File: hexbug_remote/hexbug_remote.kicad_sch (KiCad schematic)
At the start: 39 parts, among them J1 USB C, J2 Conn_01x02, J3 Conn_01x06, J4 AA, J5 AA, SW1 Tactile, SW2 Tactile, SW3 Tactile, SW4 Tactile, SW5 Tactile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

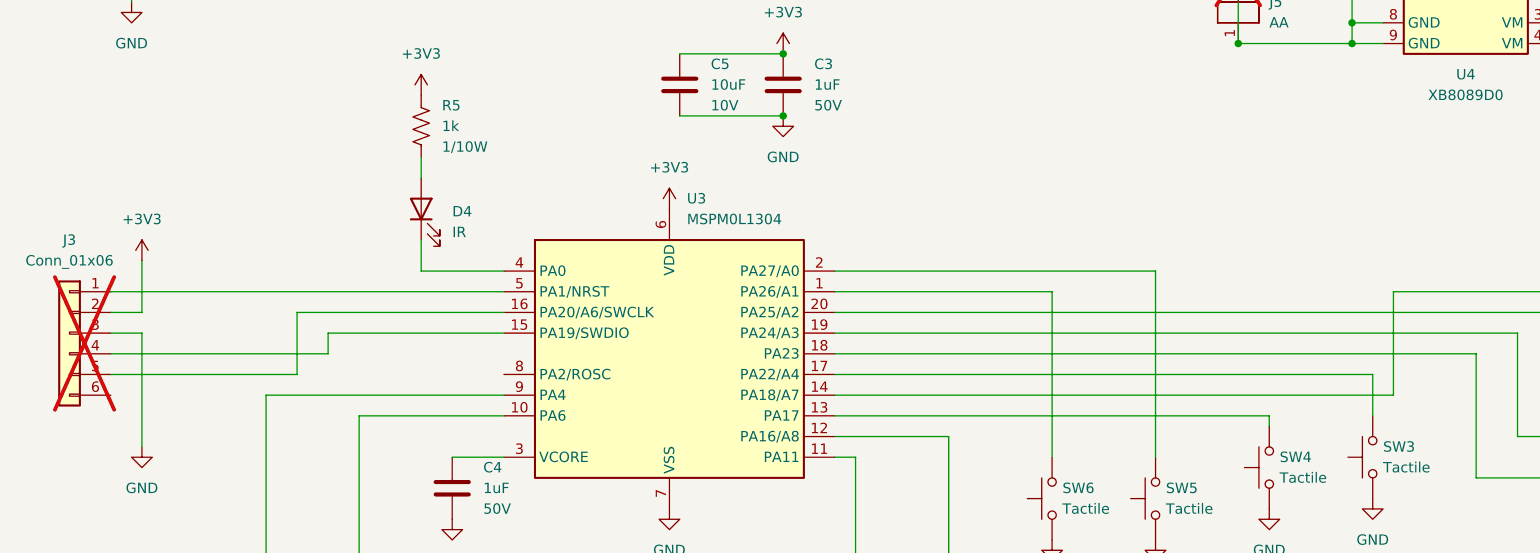
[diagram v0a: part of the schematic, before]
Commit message: Add Firmware Update PCB to Rev 2 --Pull up resistor for reset
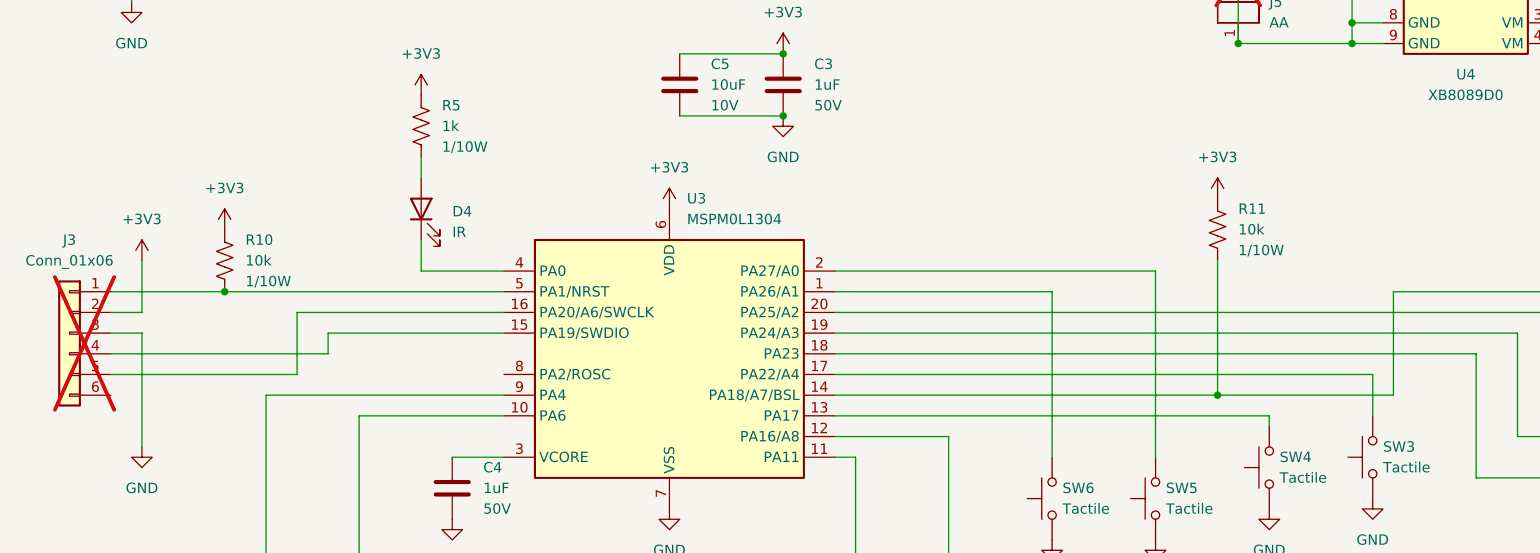
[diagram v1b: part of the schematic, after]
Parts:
- added R10, R11: 10k, Resistor_SMD:R_0603_1608Metric_Pad0.98x0.95mm_HandSolder, symbol -Local_Lib:Resistors/RES-000010
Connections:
- net +3V3: now also R10.1, R11.1
- net at SW7.1, U3.14 (PA18/A7/BSL): now also R11.2
- net at J3.1 (Pin_1), U3.5 (PA1/NRST): now also R10.2
